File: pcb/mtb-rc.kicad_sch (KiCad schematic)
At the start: 39 parts, among them J1 MVE252-5-V, J2 MVE252-5-V, J9 MVE252-5-V, U1 VO0631T, U2 VO0631T, U3 VO0631T

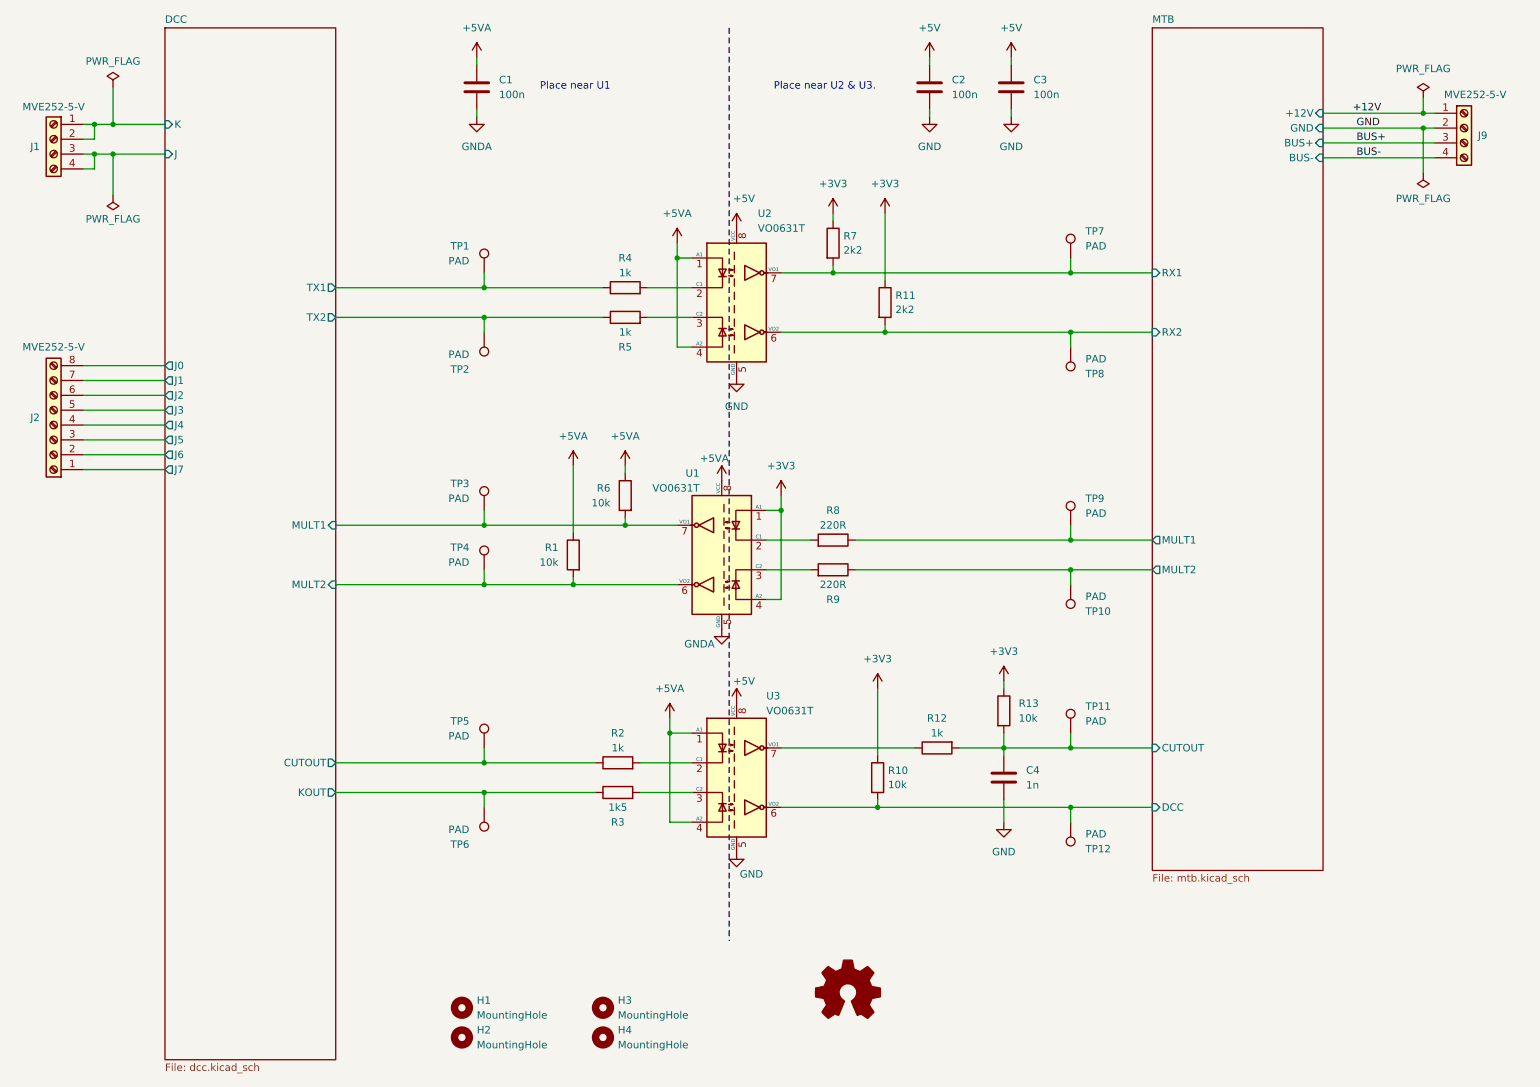
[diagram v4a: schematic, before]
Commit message: Add optocoupler-led protection diode. Close #1.
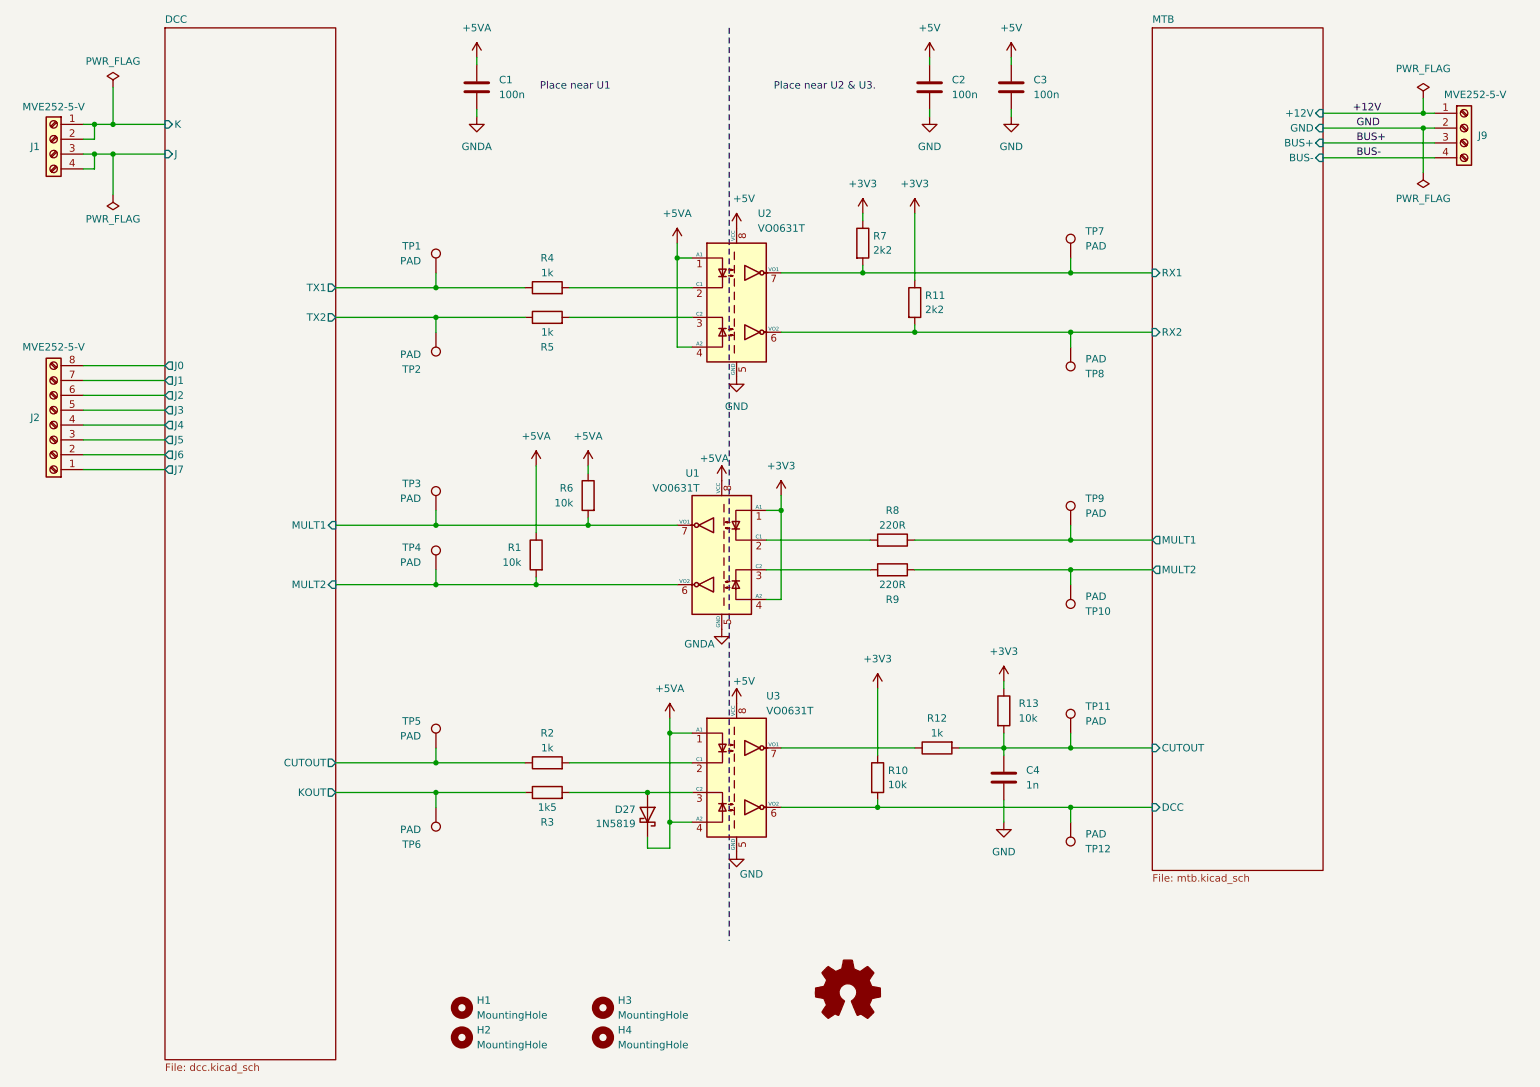
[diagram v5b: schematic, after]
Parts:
- added D27: 1N5819, Diode_SMD:D_SOD-123, symbol Device:D_Schottky
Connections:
- net +5VA: now also D27.1 (K)
- net at R3.2, U3.3 (C2): now also D27.2 (A)
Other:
- moved on the sheet: R1, R11, R2, R3, R4, R5, R6, R7, R8, R9, TP1, TP2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

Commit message: Remove "PAD" value of testpads where pads are not used.
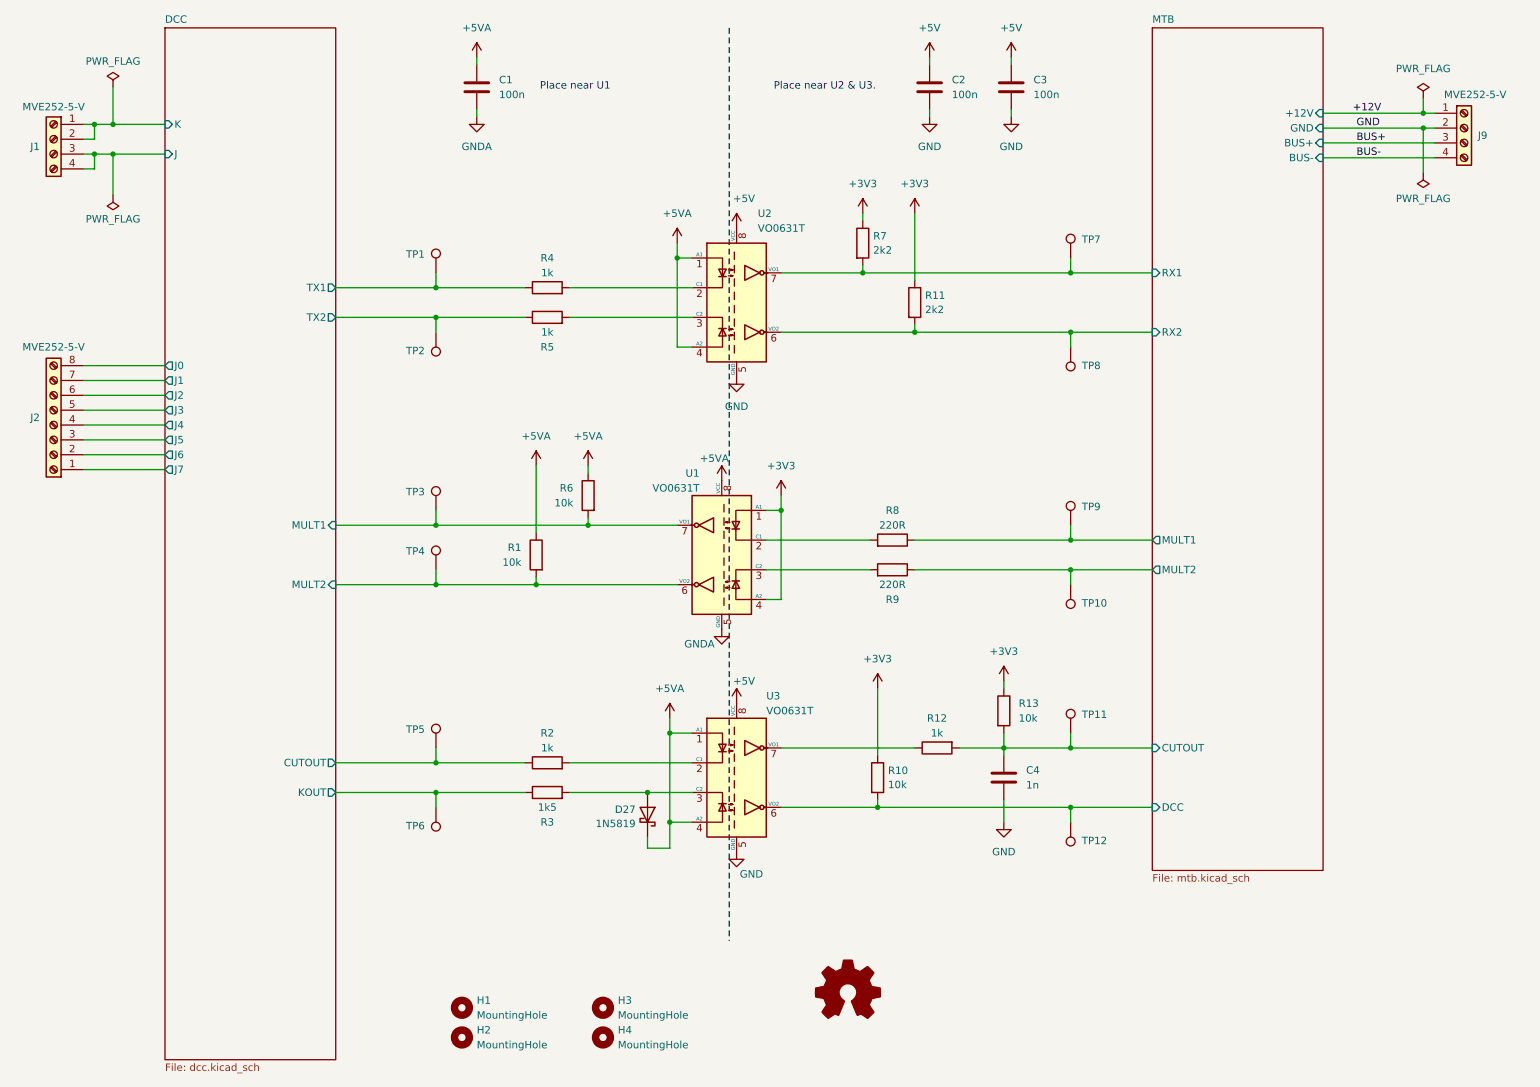
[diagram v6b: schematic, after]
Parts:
- TP1, TP10, TP11, TP12, TP2, TP3, TP4, TP5, TP6, TP7, TP8, TP9: value PAD -> ~
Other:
- moved on the sheet: TP12
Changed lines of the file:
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@@
   (symbol (lib_id "Connector:TestPoint") (at 94.615 139.7 0) (mirror y) (unit 1)
     (in_bom yes) (on_board yes) (dnp no)
-    (property "Reference" "TP5" (at 92.075 135.128 0)
-      (effects (font (size 1.27 1.27)) (justify left))
-    )
-    (property "Value" "PAD" (at 92.075 137.668 0)
+    (property "Reference" "TP5" (at 92.71 136.525 0)
+      (effects (font (size 1.27 1.27)) (justify left))
+    )
+    (property "Value" "~" (at 92.075 137.668 0)
       (effects (font (size 1.27 1.27)) (justify left))
     )
@@
   )
   (symbol (lib_id "Connector:TestPoint") (at 203.2 137.16 0) (unit 1)
-    (in_bom yes) (on_board yes) (dnp no) (fields_autoplaced)
-    (property "Reference" "TP11" (at 205.74 132.588 0)
-      (effects (font (size 1.27 1.27)) (justify left))
-    )
-    (property "Value" "PAD" (at 205.74 135.128 0)
+    (in_bom yes) (on_board yes) (dnp no)
+    (property "Reference" "TP11" (at 205.105 133.985 0)
+      (effects (font (size 1.27 1.27)) (justify left))
+    )
+    (property "Value" "~" (at 205.74 135.128 0)
       (effects (font (size 1.27 1.27)) (justify left))
     )
@@
   (symbol (lib_id "Connector:TestPoint") (at 94.615 58.42 0) (mirror y) (unit 1)
     (in_bom yes) (on_board yes) (dnp no)
-    (property "Reference" "TP1" (at 92.075 53.848 0)
-      (effects (font (size 1.27 1.27)) (justify left))
-    )
-    (property "Value" "PAD" (at 92.075 56.388 0)
+    (property "Reference" "TP1" (at 92.71 55.245 0)
+      (effects (font (size 1.27 1.27)) (justify left))
+    )
+    (property "Value" "~" (at 92.075 56.388 0)
       (effects (font (size 1.27 1.27)) (justify left))
     )
@@
     )
   )
-  (symbol (lib_id "Connector:TestPoint") (at 203.2 152.4 0) (mirror x) (unit 1)
-    (in_bom yes) (on_board yes) (dnp no) (fields_autoplaced)
-    (property "Reference" "TP12" (at 205.74 156.972 0)
-      (effects (font (size 1.27 1.27)) (justify left))
-    )
-    (property "Value" "PAD" (at 205.74 154.432 0)
-      (effects (font (size 1.27 1.27)) (justify left))
-    )
-    (property "Footprint" "Connector_PinHeader_2.54mm:PinHeader_1x01_P2.54mm_Vertical" (at 208.28 152.4 0)
-      (effects (font (size 1.27 1.27)) hide)
-    )
-    (property "Datasheet" "~" (at 208.28 152.4 0)
+  (symbol (lib_id "Connector:TestPoint") (at 203.2 152.4 180) (unit 1)
+    (in_bom yes) (on_board yes) (dnp no)
+    (property "Reference" "TP12" (at 205.105 155.575 0)
+      (effects (font (size 1.27 1.27)) (justify right))
+    )
+    (property "Value" "~" (at 200.66 154.432 0)
+      (effects (font (size 1.27 1.27)) (justify left))
+    )
+    (property "Footprint" "Connector_PinHeader_2.54mm:PinHeader_1x01_P2.54mm_Vertical" (at 198.12 152.4 0)
+      (effects (font (size 1.27 1.27)) hide)
+    )
+    (property "Datasheet" "~" (at 198.12 152.4 0)
       (effects (font (size 1.27 1.27)) hide)
     )
@@
   (symbol (lib_id "Connector:TestPoint") (at 94.615 99.06 0) (mirror y) (unit 1)
     (in_bom yes) (on_board yes) (dnp no)
-    (property "Reference" "TP3" (at 92.075 94.488 0)
-      (effects (font (size 1.27 1.27)) (justify left))
-    )
-    (property "Value" "PAD" (at 92.075 97.028 0)
+    (property "Reference" "TP3" (at 92.71 95.885 0)
+      (effects (font (size 1.27 1.27)) (justify left))
+    )
+    (property "Value" "~" (at 92.075 97.028 0)
       (effects (font (size 1.27 1.27)) (justify left))
     )
@@
   (symbol (lib_id "Connector:TestPoint") (at 94.615 68.58 180) (unit 1)
     (in_bom yes) (on_board yes) (dnp no)
-    (property "Reference" "TP2" (at 92.075 74.93 0)
-      (effects (font (size 1.27 1.27)) (justify left))
-    )
-    (property "Value" "PAD" (at 92.075 72.39 0)
+    (property "Reference" "TP2" (at 92.71 71.755 0)
+      (effects (font (size 1.27 1.27)) (justify left))
+    )
+    (property "Value" "~" (at 92.075 72.39 0)
       (effects (font (size 1.27 1.27)) (justify left))
     )
@@
   (symbol (lib_id "Connector:TestPoint") (at 203.2 71.12 0) (mirror x) (unit 1)
     (in_bom yes) (on_board yes) (dnp no)
-    (property "Reference" "TP8" (at 205.74 75.692 0)
-      (effects (font (size 1.27 1.27)) (justify left))
-    )
-    (property "Value" "PAD" (at 205.74 73.152 0)
+    (property "Reference" "TP8" (at 205.105 74.295 0)
+      (effects (font (size 1.27 1.27)) (justify left))
+    )
+    (property "Value" "~" (at 205.74 73.152 0)
       (effects (font (size 1.27 1.27)) (justify left))
     )
@@
   (symbol (lib_id "Connector:TestPoint") (at 94.615 149.86 180) (unit 1)
     (in_bom yes) (on_board yes) (dnp no)
-    (property "Reference" "TP6" (at 92.075 156.21 0)
-      (effects (font (size 1.27 1.27)) (justify left))
-    )
-    (property "Value" "PAD" (at 92.075 153.67 0)
+    (property "Reference" "TP6" (at 92.71 153.035 0)
+      (effects (font (size 1.27 1.27)) (justify left))
+    )
+    (property "Value" "~" (at 92.075 153.67 0)
       (effects (font (size 1.27 1.27)) (justify left))
     )
@@
   )
   (symbol (lib_id "Connector:TestPoint") (at 203.2 101.6 0) (unit 1)
-    (in_bom yes) (on_board yes) (dnp no) (fields_autoplaced)
-    (property "Reference" "TP9" (at 205.74 97.028 0)
-      (effects (font (size 1.27 1.27)) (justify left))
-    )
-    (property "Value" "PAD" (at 205.74 99.568 0)
+    (in_bom yes) (on_board yes) (dnp no)
+    (property "Reference" "TP9" (at 205.105 98.425 0)
+      (effects (font (size 1.27 1.27)) (justify left))
+    )
+    (property "Value" "~" (at 205.74 99.568 0)
       (effects (font (size 1.27 1.27)) (justify left))
     )
@@
   )
   (symbol (lib_id "Connector:TestPoint") (at 203.2 55.88 0) (unit 1)
-    (in_bom yes) (on_board yes) (dnp no) (fields_autoplaced)
-    (property "Reference" "TP7" (at 205.74 51.308 0)
-      (effects (font (size 1.27 1.27)) (justify left))
-    )
-    (property "Value" "PAD" (at 205.74 53.848 0)
+    (in_bom yes) (on_board yes) (dnp no)
+    (property "Reference" "TP7" (at 205.105 52.705 0)
+      (effects (font (size 1.27 1.27)) (justify left))
+    )
+    (property "Value" "~" (at 205.74 53.848 0)
       (effects (font (size 1.27 1.27)) (justify left))
     )
@@
   (symbol (lib_id "Connector:TestPoint") (at 203.2 111.76 0) (mirror x) (unit 1)
     (in_bom yes) (on_board yes) (dnp no)
-    (property "Reference" "TP10" (at 205.74 116.332 0)
-      (effects (font (size 1.27 1.27)) (justify left))
-    )
-    (property "Value" "PAD" (at 205.74 113.792 0)
+    (property "Reference" "TP10" (at 205.105 114.935 0)
+      (effects (font (size 1.27 1.27)) (justify left))
+    )
+    (property "Value" "~" (at 205.74 113.792 0)
       (effects (font (size 1.27 1.27)) (justify left))
     )
@@
   (symbol (lib_id "Connector:TestPoint") (at 94.615 109.22 0) (unit 1)
     (in_bom yes) (on_board yes) (dnp no)
-    (property "Reference" "TP4" (at 92.075 105.41 0)
+    (property "Reference" "TP4" (at 92.71 106.045 0)
       (effects (font (size 1.27 1.27)) (justify right))
     )
-    (property "Value" "PAD" (at 92.075 107.95 0)
+    (property "Value" "~" (at 92.075 107.95 0)
       (effects (font (size 1.27 1.27)) (justify right))
     )
